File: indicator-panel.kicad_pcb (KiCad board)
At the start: 2 copper layers, 133.1 x 77.2 mm, 77 parts, among them J101 Power In, P101 Data In, P102 Data Out, P103 Power In, P104 Power Out, U101 MAX3293, U102 STP16CP05, U103 STP16CP05, U106 STP16CP05, U108 LD1117S33CTR, U109 MAX3280, U110 MAX3280, U111 MAX3280

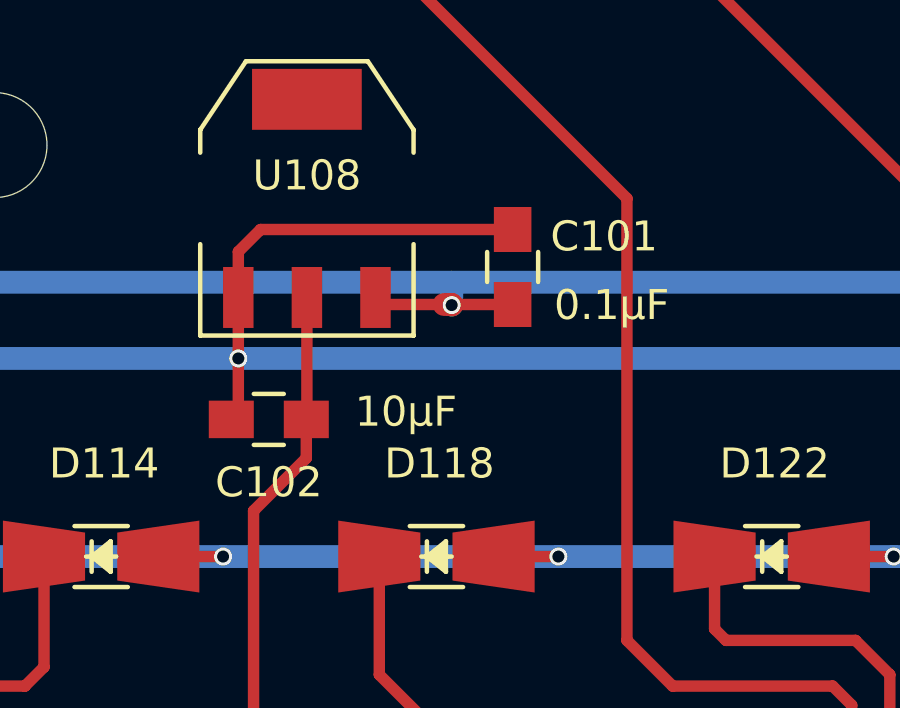
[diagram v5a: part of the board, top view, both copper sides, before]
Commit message: Added barrel connector and shrunk schematic to Letter size.  Last update before changing to add Blank and Board Detect signals.
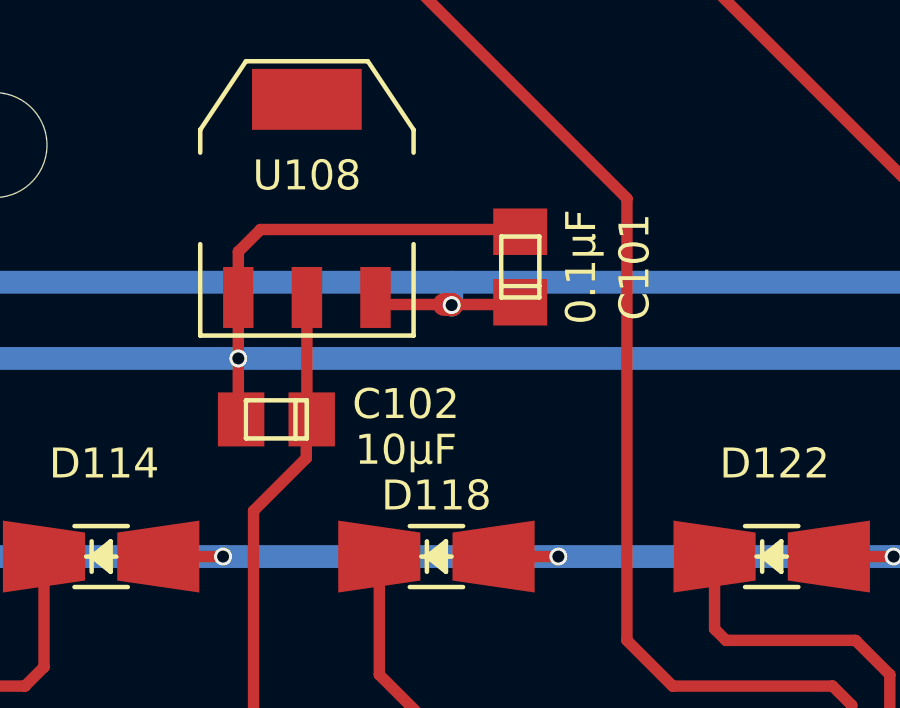
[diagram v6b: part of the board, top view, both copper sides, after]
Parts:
- C101, C102: footprint Capacitors_SMD:C_0805_HandSoldering -> Capacitors_Tantalum_SMD:TantalC_SizeR_EIA-2012
- P101: footprint Pin_Header_Angled_2x04 -> Pin_Headers:Pin_Header_Angled_2x04
- P103: footprint Pin_Header_Angled_2x05 -> Pin_Headers:Pin_Header_Angled_2x05
- moved C101 0.25 mm to (109.0, 75.2), turned to 270 degrees
- moved C102 0.25 mm to (100.8, 80.3), turned to 0 degrees

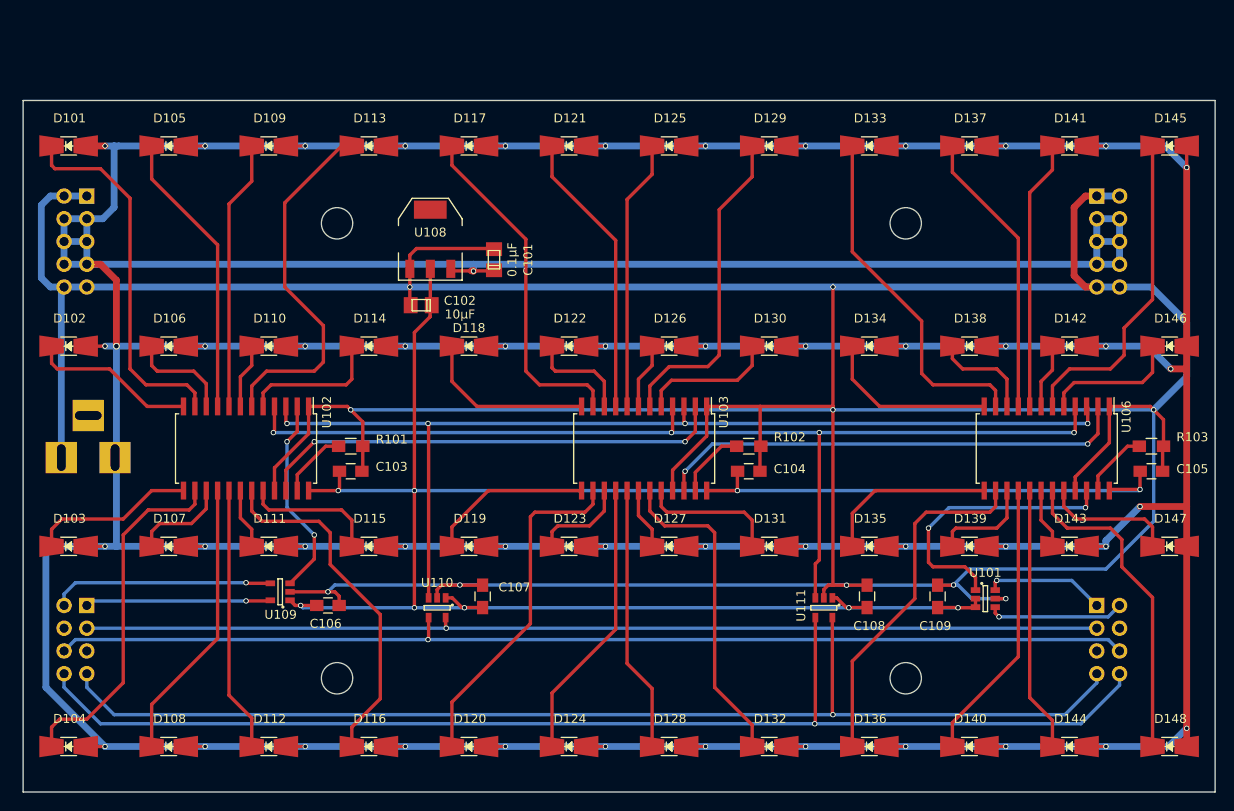
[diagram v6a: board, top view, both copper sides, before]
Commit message: Changed to version 2.0 with the blanking signal and using a 4-unit rs485 receiver and transmitter.
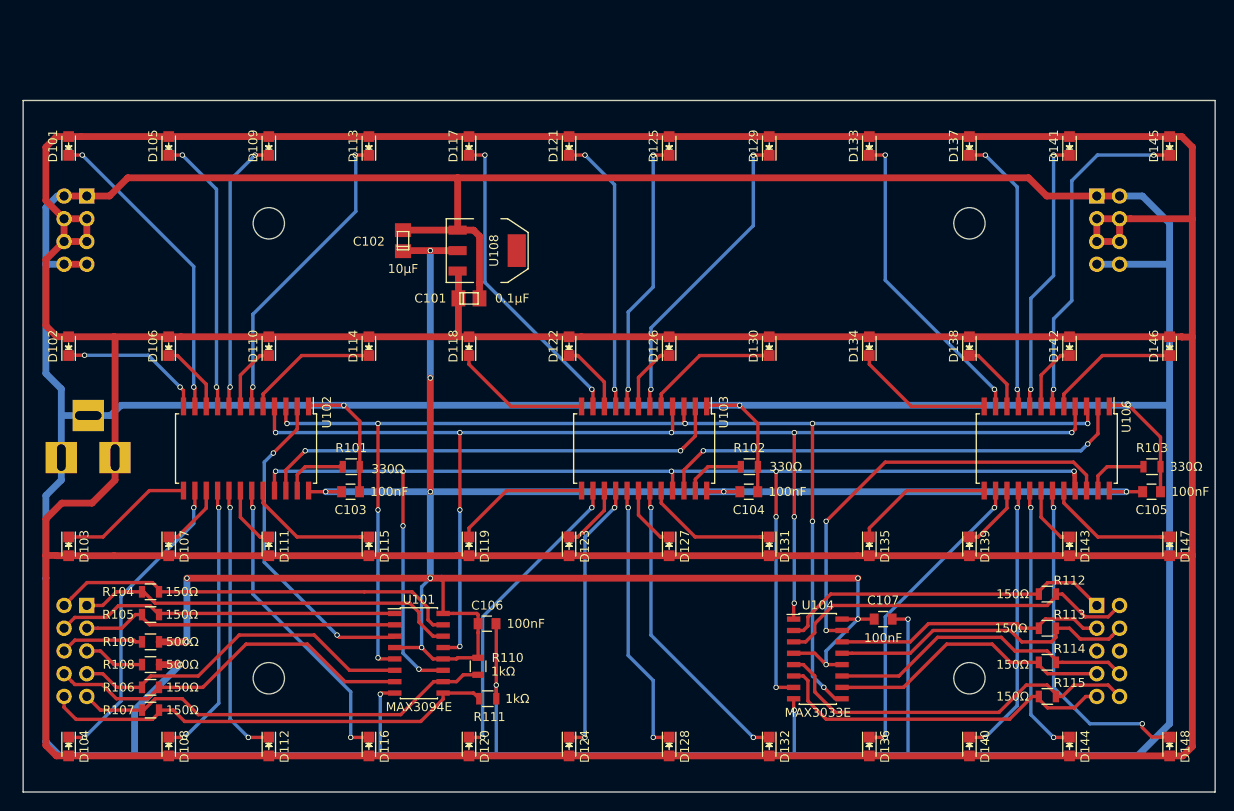
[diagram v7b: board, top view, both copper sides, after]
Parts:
- removed C108, C109: 100nF, Capacitors_SMD:C_0805_HandSoldering
- removed U109, U110, U111: MAX3280, TO_SOT_Packages_SMD:SOT-23-5
- added R104: 150Ω, Resistors_SMD:R_0805, F.Cu at (70.6, 112.3)
- added R105: 150Ω, Resistors_SMD:R_0805, F.Cu at (70.6, 114.8)
- added R106: 150Ω, Resistors_SMD:R_0805, F.Cu at (70.6, 122.9)
- added R107: 150Ω, Resistors_SMD:R_0805, F.Cu at (70.6, 125.5)
- added R108: 500Ω, Resistors_SMD:R_0805, F.Cu at (70.6, 120.4)
- added R109: 500Ω, Resistors_SMD:R_0805, F.Cu at (70.6, 117.9)
- added R110: 1kΩ, Resistors_SMD:R_0805, F.Cu at (107.2, 120.6)
- added R111: 1kΩ, Resistors_SMD:R_0805, F.Cu at (108.3, 124.2)
- added R112: 150Ω, Resistors_SMD:R_0805, F.Cu at (170.8, 112.5)
- added R113: 150Ω, Resistors_SMD:R_0805, F.Cu at (170.8, 116.3)
- added R114: 150Ω, Resistors_SMD:R_0805, F.Cu at (170.8, 120.1)
- added R115: 150Ω, Resistors_SMD:R_0805, F.Cu at (170.8, 124.0)
- added U104: MAX3033E, Housings_SOIC:SOIC-16_3.9x9.9mm_Pitch1.27mm, F.Cu at (145.1, 119.8)
- C103, C104, C105, C106, C107: footprint Capacitors_SMD:C_0805_HandSoldering -> Capacitors_SMD:C_0805
- D101, D102, D103, D104, D105, D106, D107, D108, D109, D110, D111, D112, D113, D114, D115, D116, D117, D118, D119, D120, D121, D122, D123, D124, D125, D126, D127, D128, D129, D130, D131, D132, D133, D134, D135, D136, D137, D138, D139, D140, D141, D142, D143, D144, D145, D146, D147, D148: footprint myMods.pretty:LED_SMDuniversal_0805to1206 -> LEDs:LED-0805
- P101: value Data In -> Data in; footprint Pin_Headers:Pin_Header_Angled_2x04 -> Pin_Headers:Pin_Header_Angled_2x05
- P102: footprint Socket_Strips:Socket_Strip_Angled_2x04 -> Socket_Strips:Socket_Strip_Angled_2x05
- P103: footprint Pin_Headers:Pin_Header_Angled_2x05 -> Pin_Headers:Pin_Header_Angled_2x04
- P104: footprint Socket_Strips:Socket_Strip_Angled_2x05 -> Socket_Strips:Socket_Strip_Angled_2x04
- R101, R102, R103: footprint Resistors_SMD:R_0805_HandSoldering -> Resistors_SMD:R_0805
- U101: value MAX3293 -> MAX3094E; footprint TO_SOT_Packages_SMD:SOT-23-6 -> Housings_SOIC:SOIC-16_3.9x9.9mm_Pitch1.27mm
- moved U101 63.5 mm to (100.6, 119.1)
- moved C107 44.8 mm to (152.4, 115.3), turned to 0 degrees
- moved C106 17.9 mm to (108.2, 115.8)
- moved REF** 7.62 mm to (83.8, 71.1)
- moved REF** 7.62 mm to (83.8, 121.9)
- moved C102 7.49 mm to (98.8, 73.1), turned to 270 degrees
- moved REF** 7.11 mm to (162.1, 121.9)
- moved REF** 7.11 mm to (162.1, 71.1)
- moved U108 6.48 mm to (108.2, 74.2), turned to 270 degrees
- moved C101 5.14 mm to (106.2, 79.5), turned to 180 degrees
- moved R101 2.29 mm to (93.0, 98.3)
- moved R102 2.29 mm to (137.5, 98.3)
- moved R103 2.29 mm to (182.4, 98.3)
- moved C103 2.29 mm to (92.9, 101.1)
- moved C105 2.29 mm to (182.4, 101.1)
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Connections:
- J101 pad 3: Net-(J101-Pad3) -> GND
- P102 pad 3: Net-(P101-Pad3) -> Net-(P102-Pad3)
- P102 pad 6: Net-(P101-Pad6) -> Net-(P102-Pad6)
- P102 pad 7: Net-(P101-Pad7) -> Net-(P102-Pad7)
- P102 pad 8: Net-(P101-Pad8) -> Net-(P102-Pad8)
- P103 pad 7: +12V -> GND
- P103 pad 8: +12V -> GND
- P104 pad 7: +12V -> GND
- P104 pad 8: +12V -> GND
- U101 pad 1: Net-(U101-Pad1) -> Net-(P101-Pad4)
- U101 pad 2: +3V3 -> Net-(P101-Pad3)
- U101 pad 3: +3V3 -> Net-(U101-Pad3)
- U101 pad 4: Net-(P102-Pad2) -> +3V3
- U101 pad 5: GND -> Net-(U101-Pad5)
- U101 pad 6: Net-(P102-Pad1) -> Net-(P101-Pad7)
- U102 pad 2: Net-(U102-Pad2) -> Net-(U101-Pad3)
- U102 pad 21: GND -> Net-(U101-Pad11)
- U102 pad 3: Net-(U102-Pad3) -> Net-(U101-Pad5)
- U102 pad 4: Net-(U102-Pad4) -> Net-(U101-Pad13)
- U103 pad 21: GND -> Net-(U101-Pad11)
- U103 pad 3: Net-(U102-Pad3) -> Net-(U101-Pad5)
- U103 pad 4: Net-(U102-Pad4) -> Net-(U101-Pad13)
- U106 pad 21: GND -> Net-(U101-Pad11)
- U106 pad 22: Net-(U101-Pad1) -> Net-(U104-Pad15)
- U106 pad 3: Net-(U102-Pad3) -> Net-(U101-Pad5)
- U106 pad 4: Net-(U102-Pad4) -> Net-(U101-Pad13)
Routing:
- net +12V: track 880.7 -> 687.3 mm, vias 50 -> 0
- net Net-(U101-Pad5): track 0.00 -> 155.9 mm, vias 0 -> 9
- net Net-(U101-Pad11): track 0.00 -> 149.5 mm, vias 0 -> 9
- net Net-(U101-Pad13): track 0.00 -> 144.6 mm, vias 0 -> 9
- net Net-(U102-Pad4): track 117.0 -> 0.00 mm, vias 4 -> 0
- net Net-(U102-Pad3): track 114.8 -> 0.00 mm, vias 4 -> 0
- net Net-(P101-Pad6): track 121.4 -> 9.28 mm, vias 1 -> 0
- net Net-(P101-Pad8): track 136.0 -> 42.3 mm, vias 1 -> 0
- net GND: track 543.8 -> 636.9 mm, vias 10 -> 8
- net Net-(P101-Pad7): track 128.9 -> 39.2 mm, vias 1 -> 0
- net Net-(P101-Pad3): track 114.0 -> 35.7 mm, vias 1 -> 0
- net Net-(P101-Pad10): track 0.00 -> 51.2 mm
- net Net-(U104-Pad15): track 0.00 -> 48.1 mm, vias 0 -> 2
- net Net-(P101-Pad9): track 0.00 -> 47.4 mm
- net +3V3: track 235.8 -> 279.9 mm, vias 9 -> 13
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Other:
- board text added: "Vintage Computer Engineering Indicator Panel IP101 v 2.0 2016-02-21"
- board text removed: "Vintage Computer Engineering Indicator Panel IP101 v 1.1 2016-01-14"

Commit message: Updated current limiting resistor to 3.3k
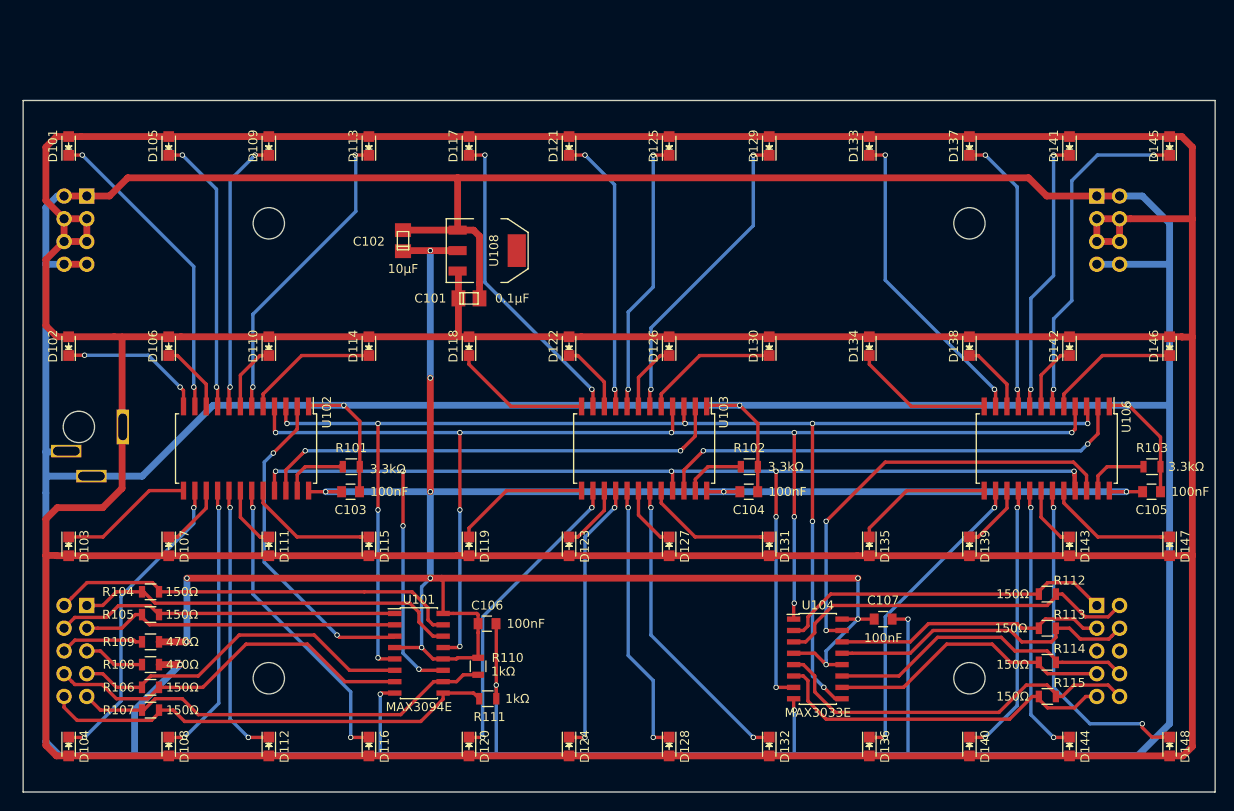
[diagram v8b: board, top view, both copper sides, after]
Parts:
- J101: footprint Connect:BARREL_JACK -> myMods.pretty:PJ-032B
- R101, R102, R103: value 330Ω -> 3.3kΩ
- R108, R109: value 500Ω -> 470Ω
- moved J101 7.85 mm to (67.5, 93.9), turned to 180 degrees
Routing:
- net GND: track 636.9 -> 642.2 mm
- net +12V: track 687.3 -> 688.5 mm
